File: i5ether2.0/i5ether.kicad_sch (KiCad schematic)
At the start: 14 parts, among them J2 Conn_02x05_Odd_Even, J3 1-406541-1, T2 HX5008

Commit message: Modulos
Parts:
- removed C10, C9: 4700p, Resistor_SMD:R_1812_4532Metric, symbol Device:C_Small
- removed C12: 1000p, Capacitor_SMD:C_0402_1005Metric, symbol Device:C_Small
- removed C2, C4, C6, C8: 0.1u, Capacitor_SMD:C_0402_1005Metric, symbol Device:C_Small
- removed J2: Conn_02x05_Odd_Even, Connector_PinHeader_2.54mm:PinHeader_2x05_P2.54mm_Vertical, symbol Connector_Generic:Conn_02x05_Odd_Even
- removed J3: 1-406541-1, MJ406541:1-406541-1, symbol MJ406541:1-406541-1
- removed R2, R4, R6, R8: 75, Resistor_SMD:R_0402_1005Metric, symbol Device:R_Small
- removed T2: HX5008, HX5008:HX5008NL, symbol HX5008:HX5008
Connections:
- no-connect marks 2 -> 0
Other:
- added sheet ethernet_module (ethernet_module.kicad_sch)

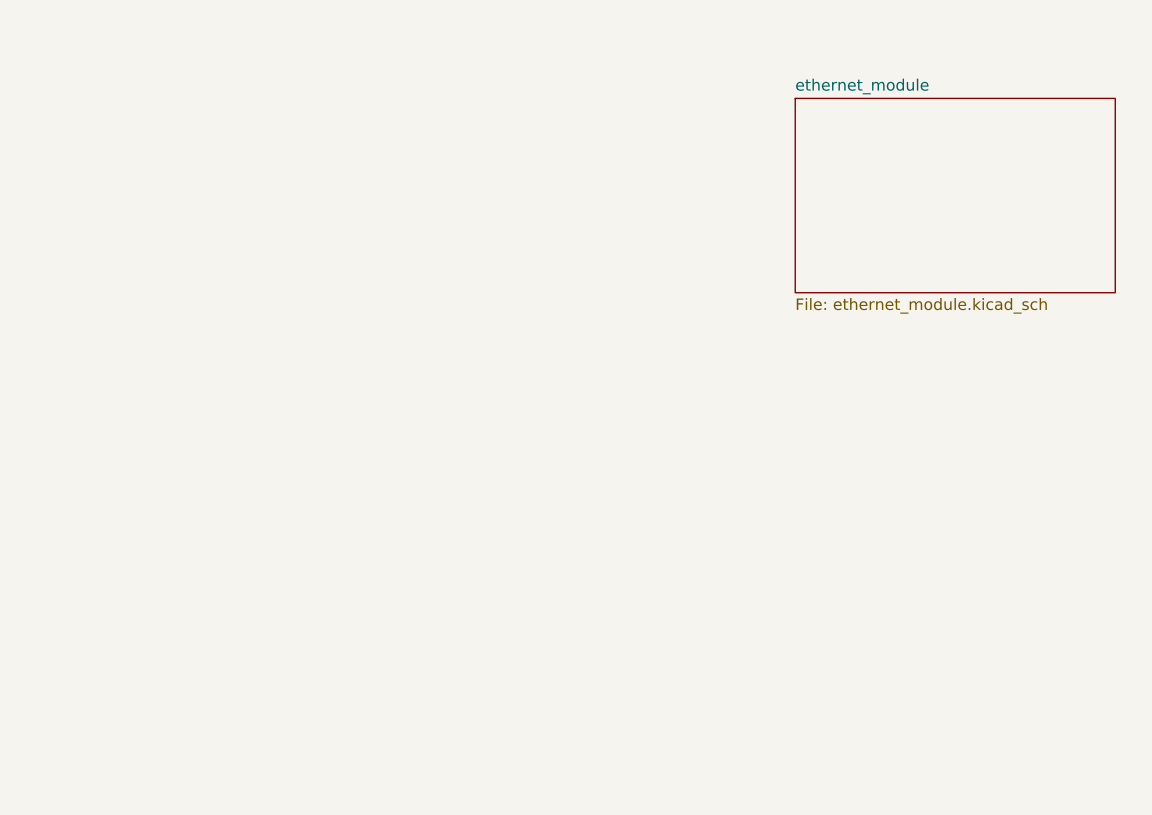
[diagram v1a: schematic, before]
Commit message: Arreglos esquematico ethernet
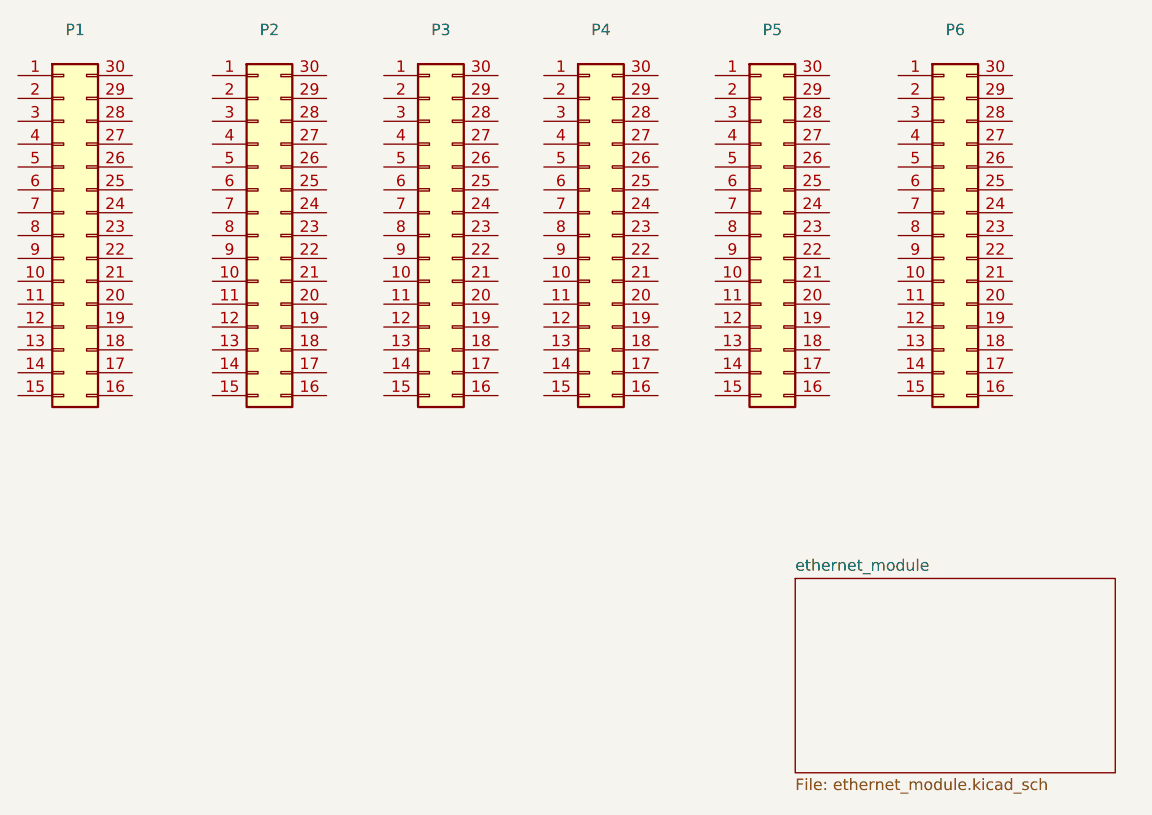
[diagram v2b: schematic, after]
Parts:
- added P1, P2, P3, P4, P5, P6: Conn_02x15_Counter_Clockwise, symbol Connector_Generic:Conn_02x15_Counter_Clockwise

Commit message: Essquematico con pantalla
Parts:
- removed P1: Conn_02x15_Counter_Clockwise, symbol Connector_Generic:Conn_02x15_Counter_Clockwise
- added P1: Conn_02x05_Counter_Clockwise, symbol Connector_Generic:Conn_02x05_Counter_Clockwise
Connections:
- net screen_module/T_IRQ: now reaches P6.16 (Pin_16)
- net screen_module/T_DO: now reaches P6.17 (Pin_17)
- net screen_module/T_DIN: now reaches P6.18 (Pin_18)
- net screen_module/T_CS: now reaches P6.19 (Pin_19)
- net screen_module/T_CLK: now reaches P6.25 (Pin_25)
- net screen_module/SDO(MISO): now reaches P6.26 (Pin_26)
- net screen_module/LED: now reaches P6.27 (Pin_27)
- net screen_module/SCK: now reaches P6.28 (Pin_28)
- net screen_module/GND: now reaches P6.29 (Pin_29)
- net screen_module/CS: now reaches P6.3 (Pin_3)
- net screen_module/VCC: now reaches P6.30 (Pin_30)
- net screen_module/RESET: now reaches P6.4 (Pin_4)
- net screen_module/DC: now reaches P6.5 (Pin_5)
- net screen_module/SDI(MOSI): now reaches P6.6 (Pin_6)
- new net ethernet_module/TD1+: P1.1 (Pin_1)
- new net ethernet_module/TD1-: P1.2 (Pin_2)
- new net ethernet_module/TD2+: P1.3 (Pin_3)
- new net ethernet_module/TD2-: P1.4 (Pin_4)
- new net ethernet_module/TD3+: P1.10 (Pin_10)
- new net ethernet_module/TD3-: P1.9 (Pin_9)
- new net ethernet_module/TD4+: P1.8 (Pin_8)
- new net ethernet_module/TD4-: P1.7 (Pin_7)
- no-connect marks 0 -> 16
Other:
- added sheet screen_module (screen_module.kicad_sch)
- sheet ethernet_module ports: added TD1+, TD1-, TD2+, TD2-, TD3+, TD3-, TD4+, TD4-; removed none
- moved on the sheet: P2, P3, P4, P5

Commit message: Avances en placa
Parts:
- removed P1: Conn_02x05_Counter_Clockwise, symbol Connector_Generic:Conn_02x05_Counter_Clockwise
- removed P5: Conn_02x15_Counter_Clockwise, symbol Connector_Generic:Conn_02x15_Counter_Clockwise
- added P1: Conn_02x15_Counter_Clockwise, Connector_PinHeader_2.54mm:PinHeader_2x15_P2.54mm_Vertical, symbol Connector_Generic:Conn_02x15_Counter_Clockwise
- P2: renamed from P6; footprint (none) -> Connector_PinHeader_2.54mm:PinHeader_2x15_P2.54mm_Vertical
- P3, P4: footprint (none) -> Connector_PinHeader_2.54mm:PinHeader_2x15_P2.54mm_Vertical
- P6: renamed from P2; footprint (none) -> Connector_PinHeader_2.54mm:PinHeader_2x15_P2.54mm_Vertical
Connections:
- net screen_module/CS: now also P2.6 (Pin_6); no longer P2.3 (Pin_3)
- net screen_module/DC: now also P2.10 (Pin_10); no longer P2.5 (Pin_5)
- net screen_module/GND: now also P2.4 (Pin_4); no longer P2.29 (Pin_29)
- net screen_module/LED: now also P2.7 (Pin_7); no longer P2.27 (Pin_27)
- net screen_module/RESET: now also P2.8 (Pin_8); no longer P2.4 (Pin_4)
- net screen_module/SCK: now also P2.5 (Pin_5); no longer P2.28 (Pin_28)
- net screen_module/SDI(MOSI): now also P2.12 (Pin_12); no longer P2.6 (Pin_6)
- net screen_module/SDO(MISO): now also P2.9 (Pin_9); no longer P2.26 (Pin_26)
- net screen_module/T_CLK: now also P2.11 (Pin_11); no longer P2.25 (Pin_25)
- net screen_module/T_CS: now also P2.24 (Pin_24); no longer P2.19 (Pin_19)
- net screen_module/T_DIN: now also P2.26 (Pin_26); no longer P2.18 (Pin_18)
- net screen_module/T_DO: now also P2.28 (Pin_28); no longer P2.17 (Pin_17)
- net screen_module/T_IRQ: now also P2.30 (Pin_30); no longer P2.16 (Pin_16)
- net screen_module/VCC: now also P2.2 (Pin_2); no longer P2.30 (Pin_30)
- net ethernet_module/GLED-: now reaches P2.23 (Pin_23)
- new net ethernet_module/RD+: P1.23 (Pin_23)
- new net ethernet_module/RD-: P1.25 (Pin_25)
- new net ethernet_module/TD+: P1.19 (Pin_19)
- new net ethernet_module/TD-: P1.21 (Pin_21)
- new net ethernet_module/YLED-: P2.25 (Pin_25)
- no-connect marks 16 -> 14
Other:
- added sheet SPI_module (SPI_module.kicad_sch)
- added sheet bluetooth_module (bluetooth_module.kicad_sch)
- sheet ethernet_module ports: added GLED-, RD+, RD-, TD+, TD-, YLED-; removed TD1+, TD1-, TD2+, TD2-, TD3+, TD3-, TD4+, TD4-
- moved on the sheet: P2

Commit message: Pcb huellas y esquematico (sin resitensias)
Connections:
- net bluetooth_module/RX: now reaches P6.6 (Pin_6)
- net bluetooth_module/TX: now reaches P6.8 (Pin_8)
- net SPI_module/RX: now reaches P4.10 (Pin_10)
- net SPI_module/CSn: now reaches P4.12 (Pin_12)
- net SPI_module/TX: now reaches P4.6 (Pin_6)
- net SPI_module/SCK: now reaches P4.8 (Pin_8)
- no-connect marks 14 -> 124
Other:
- sheet SPI_module ports: added CSn, RX, SCK, TX; removed none
- sheet bluetooth_module ports: added RX, TX; removed none
- moved on the sheet: P1, P3, P4, P6
